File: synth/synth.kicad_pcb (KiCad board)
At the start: 2 copper layers, 250 x 100 mm, 241 parts, among them J1 MEM2061-01-188-00-A, J2 10118194-0001LF, J3 PMOD_conn, J4 debug_conn, J5 AudioJack3_SwitchTR, J6 AudioJack3_SwitchTR, P1 keypad, P10 keypad, P11 keypad, P12 keypad, P13 keypad, P14 keypad, P15 keypad, P16 keypad, P17 keypad, P18 keypad, P19 keypad, P2 keypad, P20 keypad, P21 keypad, P22 keypad, P23 keypad, P24 keypad, P3 keypad, P4 keypad, P5 keypad, P6 keypad, P7 keypad, P8 keypad, P9 keypad, SW1 SW_Push, SW10 PB86-A2, SW11 PB86-A2, SW12 PB86-A2, SW13 PB86-A2, SW14 PB86-A2, SW15 PB86-A2, SW16 PB86-A2, SW17 PB86-A2, SW18 PB86-A2, SW19 PB86-A2, SW2 SW_Push, SW20 PB86-A2, SW21 PB86-A2, SW22 PB86-A2, SW23 PB86-A2, SW24 PB86-A2, SW25 PB86-A2, SW26 SW_DPDT_x2_MFS201N−16−Z, SW3 SW_Push, SW4 SW_Push, SW5 SW_Push, SW6 SW_Push, SW7 SW_Push, SW8 SW_Push, SW9 SW_Push, U1 ATSAME53N19A, U10 AD8531, U11 AD8531, U12 DS2745, U13 DSC6003JI2A, U14 LMS33460, U15 BQ24074, U16 TPS62120DCNR, U17 TPS63031, U18 STP16CPC26PTR, U19 STP16CPC26PTR, U2 DRA818_iCE40-UP5K-SG48, U3 74HC165, U4 74HC165, U5 74HC165, U6 74HC165, U7 DSC6003JI2A, U8 DS1881, U9 DS1881

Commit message: Design checkpoint for 20210715
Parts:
- removed C51, C52, C54, C55: CP_270uF_10v_PXF, up5k-synth:CP_Elec_6.3x5.8
- C19, C22, C27, C28, C30, C32: moved to B.Cu
- C56: moved to F.Cu
- moved C19 120.9 mm to (141.2, 39.6), turned to 90 degrees
- moved C30 114.4 mm to (127.6, 39.6), turned to 270 degrees
- moved C28 114.2 mm to (130.2, 38.8), turned to 270 degrees
- moved C32 113.8 mm to (118.6, 42.6), turned to 270 degrees
- moved C27 113.2 mm to (121.4, 43.0), turned to 270 degrees
- moved R77 109.9 mm to (118.8, 48.1), turned to 90 degrees
- moved C22 102.6 mm to (130.2, 53.0), turned to 270 degrees
- moved R76 96.5 mm to (125.8, 44.6), turned to 90 degrees
- moved C53 92.0 mm to (123.0, 45.8)
- moved R79 88.1 mm to (119.4, 37.2), turned to 90 degrees
- moved R78 81.1 mm to (134.0, 39.2)
- moved C56 67.2 mm to (143.9, 40.7), turned to 90 degrees
- moved R73 54.7 mm to (138.8, 52.4), turned to 270 degrees
- moved U9 48.3 mm to (134.8, 50.6), turned to 270 degrees
- moved R72 43.7 mm to (135.7, 45.1), turned to 0 degrees
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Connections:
- C27 pad 1: /OUT0_R -> /OUT0_L
- C28 pad 1: /OUT0_L -> /OUT0_R
- C30 pad 1: /OUT0_L -> /OUT0_R
- C32 pad 1: /OUT0_R -> /OUT0_L
- DIS1 pad 6: /SC4_PAD[0] -> /DISPLAY_CMD
- J1 pad 12: Net-(J1-Pad12) -> /SDHC1_SDCD
- J1 pad 13: Net-(J1-Pad13) -> GND
- R78 pad 1: /OUT0_L -> /OUT0_R
- R79 pad 1: /OUT0_R -> /OUT0_L
- U1 pad 21: /SW_DATA -> /DISPLAY_CS
- U1 pad 22: /SW_CLK -> /DISPLAY_CMD
- U1 pad 23: /SW_LOAD -> /DISPLAY_RST
- U1 pad 32: /DISPLAY_CMD -> Net-(U1-Pad32)
- U1 pad 33: /DISPLAY_CS -> Net-(U1-Pad33)
- U1 pad 72: Net-(U1-Pad72) -> /SW_LOAD
- U1 pad 73: Net-(U1-Pad73) -> /SW_DATA
- U10 pad 3: /Analog Output/BUF0_L -> /Analog Output/BUF0_R
- U10 pad 5: /Analog Output/BUF0_R -> /Analog Output/BUF0_L
- U9 pad 10: /Analog Output/F_PDM0_R -> /Analog Output/F_PDM0_L
- U9 pad 11: /Analog Output/BUF0_R -> /Analog Output/BUF0_L
- U9 pad 6: /Analog Output/BUF0_L -> /Analog Output/BUF0_R
- U9 pad 8: /Analog Output/F_PDM0_L -> /Analog Output/F_PDM0_R
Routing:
- net /SC0_SCL_PAD[1]: track 0.00 -> 104.7 mm, vias 0 -> 4
- net /SC0_SDA_PAD[0]: track 0.00 -> 101.9 mm, vias 0 -> 4
- net /DISPLAY_CS: track 0.00 -> 36.9 mm
- net /DISPLAY_CMD: track 0.00 -> 33.6 mm
- net /DISPLAY_RST: track 0.00 -> 30.5 mm
- net +3V3: track 39.5 -> 67.9 mm
- net /Analog Output/BUF0_L: track 0.00 -> 16.1 mm
- net /OUT0_L: track 0.00 -> 15.3 mm
- net /OUT0_R: track 0.00 -> 15.2 mm
- net /SC4_PAD[0]: track 18.6 -> 33.1 mm
- net /SC4_SCK_PAD[1]: track 10.9 -> 25.1 mm
- net Net-(R66-Pad1): track 0.00 -> 13.8 mm
- net Net-(R67-Pad1): track 0.00 -> 13.5 mm
- net /OUT1_R: track 0.00 -> 12.8 mm
- net /OUT1_L: track 0.00 -> 11.2 mm
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
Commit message: Design checkpoint on 20210716
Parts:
- R15, R16, SW1: moved to F.Cu
- R58, R8: moved to B.Cu
- moved SW1 175.1 mm to (219.1, 31.3)
- moved R16 30.0 mm to (162.4, 33.6), turned to 180 degrees
- moved R15 28.7 mm to (156.0, 36.5), turned to 270 degrees
- moved R58 17.9 mm to (227.1, 29.7)
- moved R55 15.1 mm to (226.0, 37.1), turned to 180 degrees
- moved SW24 10.0 mm to (250.5, 69.8)
- moved SW25 10.0 mm to (260.5, 69.8)
- moved R6 6.48 mm to (264.0, 37.7), turned to 90 degrees
- moved U3 2.20 mm to (233.4, 33.9)
- moved C18 0.31 mm to (268.3, 37.5)
- turned U4 to 180 degrees
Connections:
- U1 pad 32: Net-(U1-Pad32) -> /SW_DATA
- U1 pad 72: /SW_LOAD -> Net-(U1-Pad72)
- U1 pad 73: /SW_DATA -> Net-(U1-Pad73)
- U1 pad 78: /SEQ_OE -> /SW_LOAD
- U1 pad 79: /SEQ_LE -> /SW_CLK
- U1 pad 83: Net-(U1-Pad83) -> /SEQ_OE
- U1 pad 84: Net-(U1-Pad84) -> /SEQ_LE
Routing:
- net /IO/RLED_8: track 0.00 -> 101.8 mm, vias 0 -> 1
- net /IO/RLED_9: track 0.00 -> 93.8 mm, vias 0 -> 1
- net /IO/RLED_10: track 0.00 -> 84.0 mm, vias 0 -> 1
- net /IO/RLED_11: track 0.00 -> 71.7 mm, vias 0 -> 1
- net /IO/RLED_0: track 0.00 -> 62.0 mm
- net /IO/RLED_12: track 0.00 -> 59.8 mm, vias 0 -> 1
- net /IO/RLED_1: track 0.00 -> 55.6 mm, vias 0 -> 1
- net /IO/RLED_13: track 0.00 -> 54.1 mm, vias 0 -> 1
- net /IO/SW_BTN0: track 0.00 -> 49.1 mm, vias 0 -> 1
- net /IO/RLED_2: track 0.00 -> 48.7 mm, vias 0 -> 1
- net /IO/RLED_3: track 0.00 -> 42.6 mm, vias 0 -> 1
- net /IO/SW_BTN1: track 0.00 -> 40.4 mm, vias 0 -> 1
- net /IO/RLED_15: track 0.00 -> 38.5 mm
- net /IO/RLED_14: track 0.00 -> 37.6 mm, vias 0 -> 1
- net /IO/SW_BTN7: track 0.00 -> 36.4 mm, vias 0 -> 1
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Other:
- board text added: "Add via here if space available"

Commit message: Design checkpoint on 20210719
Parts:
- moved R59 15.5 mm to (217.9, 82.2)
- moved C42 13.9 mm to (223.2, 79.1)
- moved R5 3.42 mm to (216.7, 87.9), turned to 270 degrees
- moved C17 3.33 mm to (211.5, 93.0)
- moved U4 0.70 mm to (224.2, 86.5)
- moved C3 0.46 mm to (180.5, 56.1)
- moved C57 0.20 mm to (71.2, 41.9)
- moved C33 0.14 mm to (138.3, 41.7)
- moved R80 0.14 mm to (136.5, 45.2)
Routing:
- net Net-(U18-Pad22): track 0.00 -> 106.2 mm
- net /SW_LOAD: track 0.00 -> 84.0 mm, vias 0 -> 2
- net /SW_CLK: track 0.00 -> 83.5 mm, vias 0 -> 2
- net /IO/GLED_7: track 0.00 -> 74.9 mm
- net /IO/GLED_15: track 0.00 -> 72.5 mm
- net /IO/GLED_6: track 0.00 -> 72.0 mm
- net /IO/GLED_5: track 0.00 -> 62.4 mm
- net /IO/GLED_14: track 0.00 -> 60.4 mm
- net Net-(U3-Pad9): track 0.00 -> 59.5 mm, vias 0 -> 2
- net /IO/GLED_4: track 0.00 -> 56.3 mm
- net /SEQ_OE: track 0.00 -> 55.2 mm, vias 0 -> 2
- net /SEQ_LE: track 0.00 -> 52.4 mm
- net /SEQ_CLK: track 0.00 -> 51.6 mm
- net /IO/GLED_3: track 0.00 -> 51.3 mm
- net /SEQ_DATA: track 0.00 -> 51.0 mm, vias 0 -> 2
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
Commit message: Design checkpoint on 20210721
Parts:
- C16, C20, C21, C23, C25, C29, C31, C34, C36, C41, C43, C44, C63, R11, R19, R21, R24, R26, R3, R60, R61, R62, R63, R9: moved to B.Cu
- C24: moved to F.Cu
- moved C41 250.8 mm to (230.1, 27.0)
- moved R8 198.4 mm to (49.2, 73.1)
- moved C26 177.4 mm to (155.9, 45.2), turned to 180 degrees
- moved C63 155.7 mm to (112.3, 51.9), turned to 180 degrees
- moved C44 141.3 mm to (100.8, 67.2)
- moved C25 140.8 mm to (129.1, 57.5)
- moved R14 134.4 mm to (170.3, 81.6)
- moved C34 120.6 mm to (41.4, 63.9), turned to 90 degrees
- moved R61 117.1 mm to (99.4, 71.4), turned to 0 degrees
- moved R63 116.6 mm to (81.3, 67.8)
- moved C20 108.5 mm to (47.2, 65.4), turned to 270 degrees
- moved R26 106.8 mm to (54.7, 54.7), turned to 90 degrees
- moved R62 103.2 mm to (89.8, 80.6)
- moved C43 102.6 mm to (49.4, 79.1)
- moved C36 87.7 mm to (64.7, 83.0)
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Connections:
- R63 pad 1: /IO/SW_ENC1 -> /IO/SW_ENC2
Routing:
- net +3V3: track 107.1 -> 422.0 mm, vias 3 -> 10
- net +1V2: track 31.7 -> 62.4 mm
- net Net-(C60-Pad2): track 0.00 -> 8.19 mm
- net /PMOD[5]: track 0.00 -> 6.12 mm, vias 0 -> 1
- net /PMOD[4]: track 0.00 -> 6.08 mm, vias 0 -> 1
- net /MII_GCOL: track 29.9 -> 33.9 mm
- net Net-(R55-Pad1): track 0.00 -> 3.94 mm
- net Net-(R94-Pad1): track 0.00 -> 3.60 mm
- net Net-(L1-Pad1): track 0.00 -> 2.78 mm
- net Net-(R90-Pad1): track 0.00 -> 2.76 mm
- net GND: track 137.5 -> 135.5 mm
- net /CDONE: track 72.4 -> 71.4 mm
- net /PMOD[7]: track 0.00 -> 0.85 mm
- net /SC0_SCL_PAD[1]: track 104.7 -> 105.5 mm

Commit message: Design checkpoint on 20210726
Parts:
- removed D15, D16, D17, D18: WS2812B, up5k-synth:LED_WS2812B_PLCC4_5.0x5.0mm_P3.2mm
- R14, R27, R28, R29, R30, R31, R32, R33, R34, R35, R36, R37, R38, R39, R40, R41, R42, R43, R44, R45, R46, R47, R48, R49, R50: moved to B.Cu
- moved R32 200.3 mm to (243.6, 92.3)
- moved R28 191.9 mm to (258.5, 97.8), turned to 0 degrees
- moved R30 182.9 mm to (248.6, 110.1)
- moved R47 182.2 mm to (220.5, 98.8)
- moved R34 181.0 mm to (230.7, 109.9)
- moved R49 160.2 mm to (212.6, 116.3)
- moved R50 152.0 mm to (201.7, 97.8)
- moved R48 146.7 mm to (193.5, 115.8)
- moved R27 130.5 mm to (182.3, 97.7)
- moved R36 123.6 mm to (164.5, 93.1)
- moved R29 113.9 mm to (174.3, 116.6)
- moved R38 105.1 mm to (155.4, 110.9)
- moved R40 89.3 mm to (144.9, 97.0), turned to 0 degrees
- moved R42 76.3 mm to (136.1, 108.2)
- moved R44 73.1 mm to (125.5, 95.6), turned to 0 degrees
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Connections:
- C58 pad 2: /Power Supply/Vout -> /Vout
- C62 pad 1: /Power Supply/Vout -> /Vout
- P1 pad 2: /ADC0IN[0] -> /ADC0IN[11]
- P10 pad 2: /ADC1IN[6] -> /ADC0IN[2]
- P11 pad 2: /ADC0IN[7] -> /ADC1IN[9]
- P12 pad 2: /ADC1IN[7] -> /ADC1IN[8]
- P13 pad 2: /ADC0IN[8] -> /ADC1IN[7]
- P14 pad 2: /ADC1IN[8] -> /ADC1IN[6]
- P15 pad 2: /ADC0IN[9] -> /ADC0IN[1]
- P16 pad 2: /ADC1IN[9] -> /ADC0IN[0]
- P17 pad 2: /ADC0IN[10] -> /ADC1IN[4]
- P18 pad 2: /ADC0IN[2] -> /ADC1IN[5]
- P19 pad 2: /ADC0IN[11] -> /ADC1IN[11]
- P2 pad 2: /ADC1IN[5] -> /ADC0IN[10]
- P20 pad 2: /ADC0IN[3] -> /ADC1IN[10]
- P3 pad 2: /ADC0IN[1] -> /ADC0IN[9]
- P4 pad 2: /ADC1IN[11] -> /ADC0IN[8]
- P5 pad 2: /ADC0IN[4] -> /ADC0IN[7]
- P6 pad 2: /ADC1IN[4] -> /ADC0IN[6]
- P8 pad 2: /ADC1IN[10] -> /ADC0IN[4]
- P9 pad 2: /ADC0IN[6] -> /ADC0IN[3]
- R85 pad 1: /Power Supply/Vout -> /Vout
- R86 pad 1: /Power Supply/Vout -> /Vout
- U15 pad 10: /Power Supply/Vout -> /Vout
- U15 pad 11: /Power Supply/Vout -> /Vout
- U15 pad 6: /Power Supply/Vout -> /Vout
- U17 pad 5: /Power Supply/Vout -> /Vout
- U6 pad 11: /IO/SW_ENC1 -> /IO/SW_ENC2
- U6 pad 12: /IO/ENC1_A -> /IO/ENC2_B
- U6 pad 13: /IO/ENC1_B -> /IO/ENC2_A
- U6 pad 3: /IO/SW_ENC2 -> /IO/SW_ENC1
- U6 pad 4: /IO/ENC2_A -> /IO/ENC1_B
- U6 pad 5: /IO/ENC2_B -> /IO/ENC1_A
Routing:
- net +3V3: track 422.0 -> 1705.4 mm, vias 10 -> 17
- net /IO/SW_BTN17: track 0.00 -> 245.1 mm, vias 0 -> 3
- net /SW_CLK: track 83.5 -> 320.5 mm, vias 2 -> 5
- net /SW_LOAD: track 84.0 -> 319.7 mm, vias 2 -> 5
- net /IO/SW_BTN23: track 0.00 -> 208.5 mm, vias 0 -> 2
- net Net-(U4-Pad9): track 0.00 -> 197.4 mm, vias 0 -> 2
- net /IO/SW_BTN20: track 0.00 -> 160.6 mm, vias 0 -> 1
- net /ADC0IN[11]: track 0.00 -> 144.6 mm, vias 0 -> 1
- net /ADC0IN[9]: track 0.00 -> 126.2 mm, vias 0 -> 1
- net /LED_OUT: track 0.00 -> 123.9 mm
- net /SEQ_CLK: track 51.6 -> 174.4 mm, vias 0 -> 2
- net /ADC0IN[10]: track 0.00 -> 120.1 mm, vias 0 -> 1
- net /SEQ_LE: track 52.4 -> 171.5 mm, vias 0 -> 2
- net /SEQ_OE: track 55.2 -> 171.7 mm, vias 2 -> 3
- net /ADC0IN[13]: track 0.00 -> 115.6 mm, vias 0 -> 1
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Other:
- board text removed: "Add via here if space available"

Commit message: Design checkpoint on 20210727
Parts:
- J3: footprint up5k-synth:PinHeader_2x06_P2.54mm_Horizontal -> up5k-synth:PinHeader_2x06_P2.54mm_Vertical
- moved J3 108.1 mm to (80.6, 55.4)
- moved R42 8.98 mm to (134.3, 117.0)
- moved R43 8.84 mm to (47.4, 98.3)
- moved R32 8.50 mm to (237.3, 98.0)
- moved R31 7.91 mm to (104.3, 98.0)
- moved R41 7.18 mm to (58.3, 116.5)
- moved R46 7.18 mm to (115.3, 116.5)
- moved R34 6.75 mm to (229.3, 116.5)
- moved R45 6.50 mm to (39.3, 116.5)
- moved R30 6.41 mm to (248.3, 116.5)
- moved R33 6.02 mm to (96.3, 116.5)
- moved R38 5.98 mm to (153.3, 116.5)
- moved R36 5.85 mm to (161.3, 98.0)
- moved R35 5.74 mm to (85.3, 98.0)
- moved R39 4.93 mm to (66.4, 98.5)
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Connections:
- J1 pad 10: GND -> Net-(J1-Pad10)
- J2 pad SH: Net-(J2-PadSH) -> GND
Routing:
- net +3V3: track 1705.4 -> 1847.9 mm, vias 17 -> 23
- net /PMOD[1]: track 0.00 -> 71.0 mm, vias 0 -> 2
- net /PMOD[0]: track 0.00 -> 70.2 mm, vias 0 -> 1
- net /PMOD[2]: track 0.00 -> 68.1 mm, vias 0 -> 1
- net /PMOD[3]: track 0.00 -> 67.3 mm, vias 0 -> 2
- net /PMOD[7]: track 0.85 -> 55.0 mm, vias 0 -> 1
- net /PMOD[6]: track 1.66 -> 55.5 mm
- net /PMOD[5]: track 6.12 -> 59.2 mm, vias 1 -> 2
- net /PMOD[4]: track 6.08 -> 59.0 mm, vias 1 -> 2
- net GND: track 129.4 -> 166.9 mm, vias 68 -> 92
- net /ADC0IN[9]: track 126.2 -> 134.7 mm, vias 1 -> 2
- net /ADC0IN[7]: track 112.3 -> 120.7 mm, vias 1 -> 2
- net /ADC0IN[11]: track 144.6 -> 152.9 mm, vias 1 -> 2
- net /dbg_rst: track 90.6 -> 98.7 mm, vias 3 -> 5
- net /IO/SW_BTN21: track 24.0 -> 32.0 mm
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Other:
- rule trace_min: 0.127 -> 0

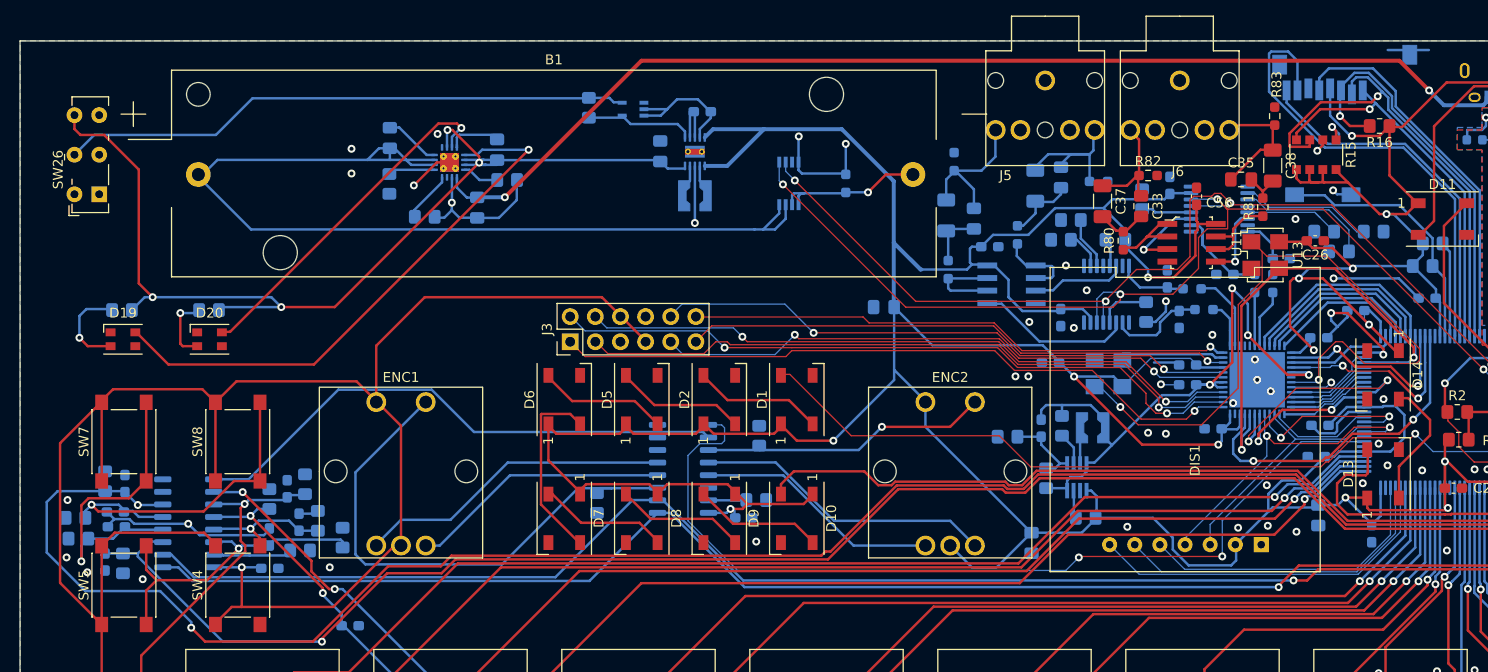
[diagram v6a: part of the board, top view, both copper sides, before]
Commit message: Update and fix power switch and battery holder footprints
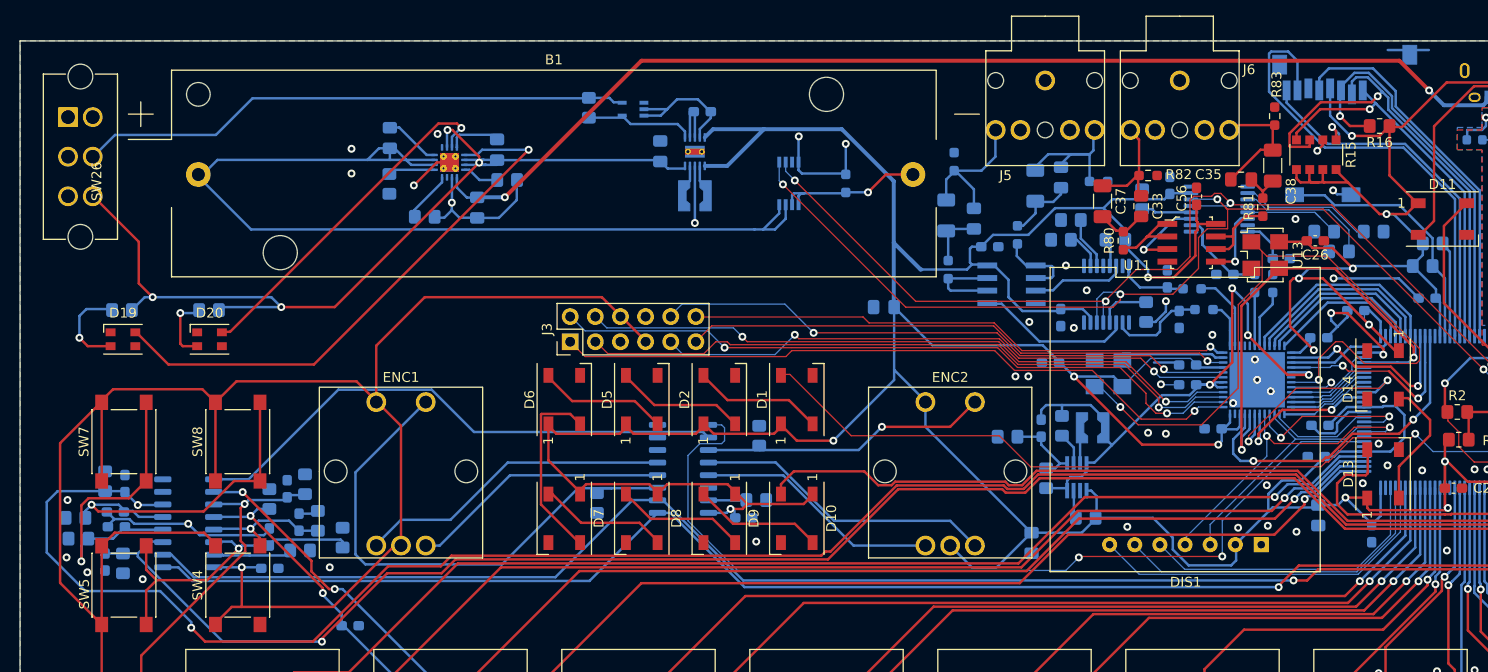
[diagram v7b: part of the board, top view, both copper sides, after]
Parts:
- moved SW26 3.85 mm to (31.1, 36.7), turned to 270 degrees
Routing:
- net /Vout: track 105.2 -> 94.8 mm
- net /PSU_EN: track 58.0 -> 56.1 mm
